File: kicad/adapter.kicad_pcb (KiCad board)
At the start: 16 copper layers, 22 x 31 mm, 14 parts

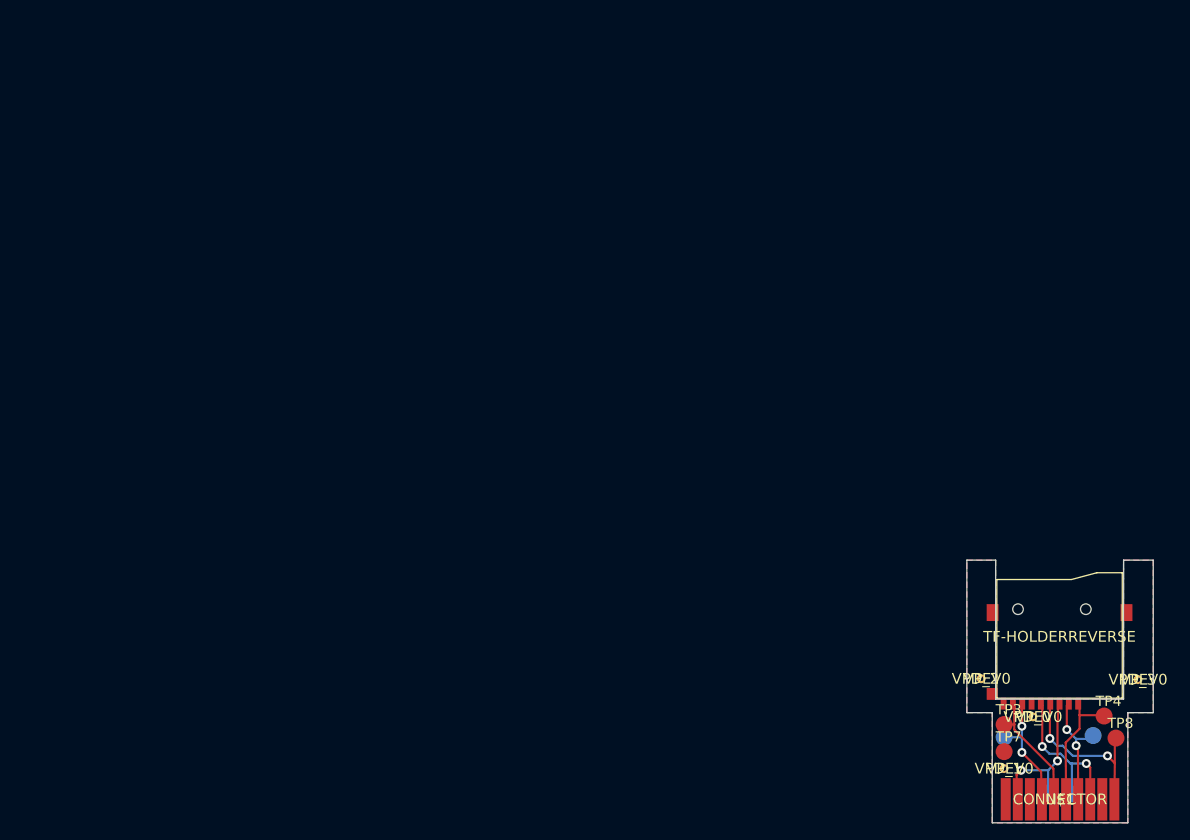
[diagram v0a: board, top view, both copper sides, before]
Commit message: Clean up automatically converted schematic.
Also generate new gerbers.
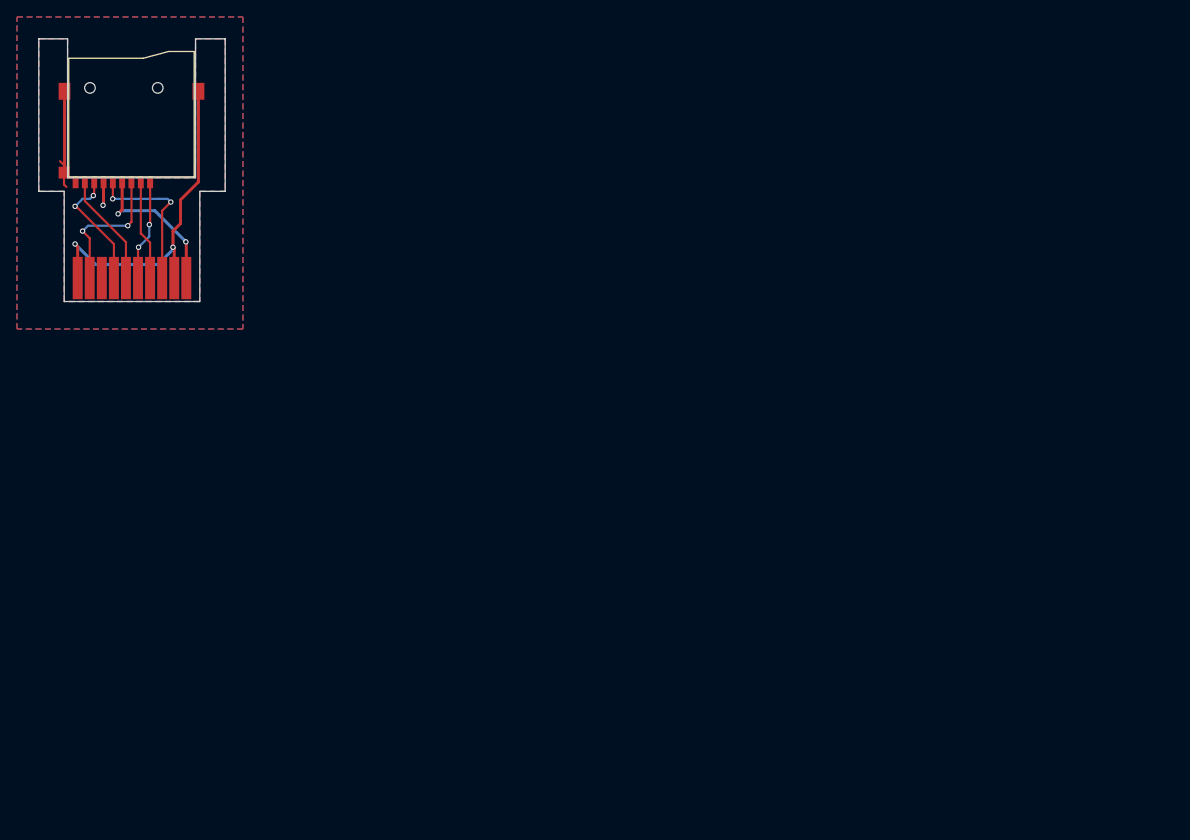
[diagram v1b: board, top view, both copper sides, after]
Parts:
- removed TP1, TP2, TP3, TP4, TP5, TP6, TP7, TP8: TPTP20R, TP20R
- removed VP_0, VP_1, VP_2, VP_3: VPDEV0, VPAC0
- C1: renamed from U$1; footprint CONNECTOR -> adapter:CONNECTOR
- moved C1 125.6 mm to (39.0, 56.2)
- moved SD1 125.6 mm to (38.9, 37.0)
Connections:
- SD1 pad 1: N$7 -> /DAT2
- SD1 pad 2: N$8 -> /DAT3
- SD1 pad 3: N$3 -> /CMD
- SD1 pad 4: N$1 -> /VCC
- SD1 pad 5: N$9 -> /CLK
- SD1 pad 7: N$5 -> /DAT0
- SD1 pad 8: N$6 -> /DAT1
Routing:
- net GND: track 0.00 -> 56.7 mm, vias 0 -> 3
- net N$1: track 20.3 -> 0.00 mm, vias 2 -> 0
- net N$9: track 19.2 -> 0.00 mm, vias 2 -> 0
- net /VCC: track 0.00 -> 18.8 mm, vias 0 -> 2
- net /CLK: track 0.00 -> 18.4 mm, vias 0 -> 2
- net N$3: track 18.0 -> 0.00 mm, vias 2 -> 0
- net /CMD: track 0.00 -> 16.8 mm, vias 0 -> 2
- net N$7: track 15.0 -> 0.00 mm
- net /DAT0: track 0.00 -> 14.7 mm, vias 0 -> 2
- net N$6: track 14.5 -> 0.00 mm
- net N$5: track 14.4 -> 0.00 mm, vias 2 -> 0
- net N$8: track 14.1 -> 0.00 mm, vias 2 -> 0
- net /DAT1: track 0.00 -> 13.3 mm
- net /DAT2: track 0.00 -> 11.9 mm, vias 0 -> 2
- net /DAT3: track 0.00 -> 11.7 mm
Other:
- net class Default: clearance 0.2 -> 0.2032; trace_width 0.25 -> 0.254; via_dia 0.6 -> 0.635; via_drill 0.4 -> 0.381
- net class Power added: clearance 0.2032, trace_width 0.3556, via_dia 0.635, via_drill 0.381
- rule trace_clearance: 0.2 -> 0.2032
- board text removed: "FillOverPAD:GND:10:30"
- board text removed: "FillOverPAD:GND:11:30"
- board text removed: "FillOverPAD:GND:12:30"
- board text removed: "FillOverPAD:GND:19:30"
- board text removed: "FillOverPAD:GND:27:30"
- board text removed: "FillOverPAD:GND:28:30"
- board text removed: "FillOverPAD:GND:29:30"
- board text removed: "FillOverPAD:GND:6:30"
- board text removed: "V:GND:1:4"
- board text removed: "V:GND:2:4"
- board text removed: "V:GND:3:4"
- board text removed: "V:GND:4:4"

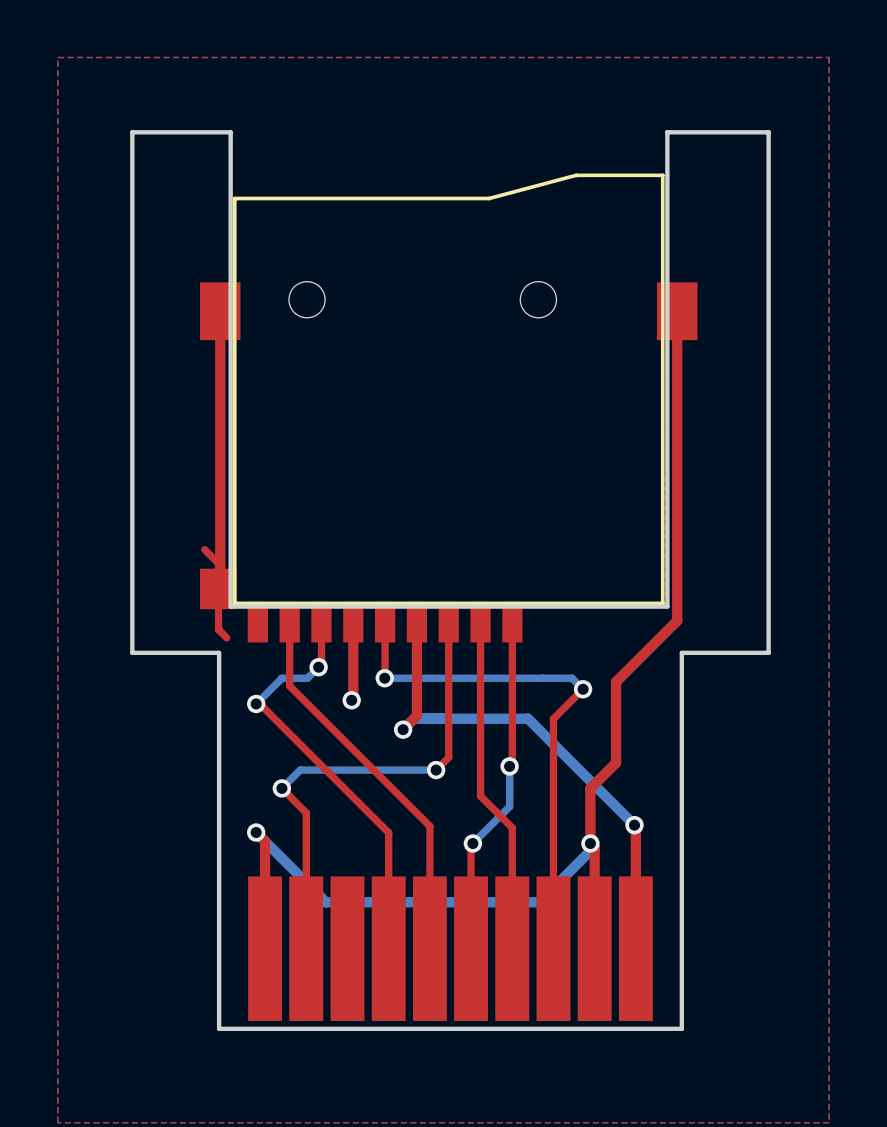
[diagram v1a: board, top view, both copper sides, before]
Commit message: Add fourth mechanical connection for SD slot.
Plus fill keepout around connector pins.
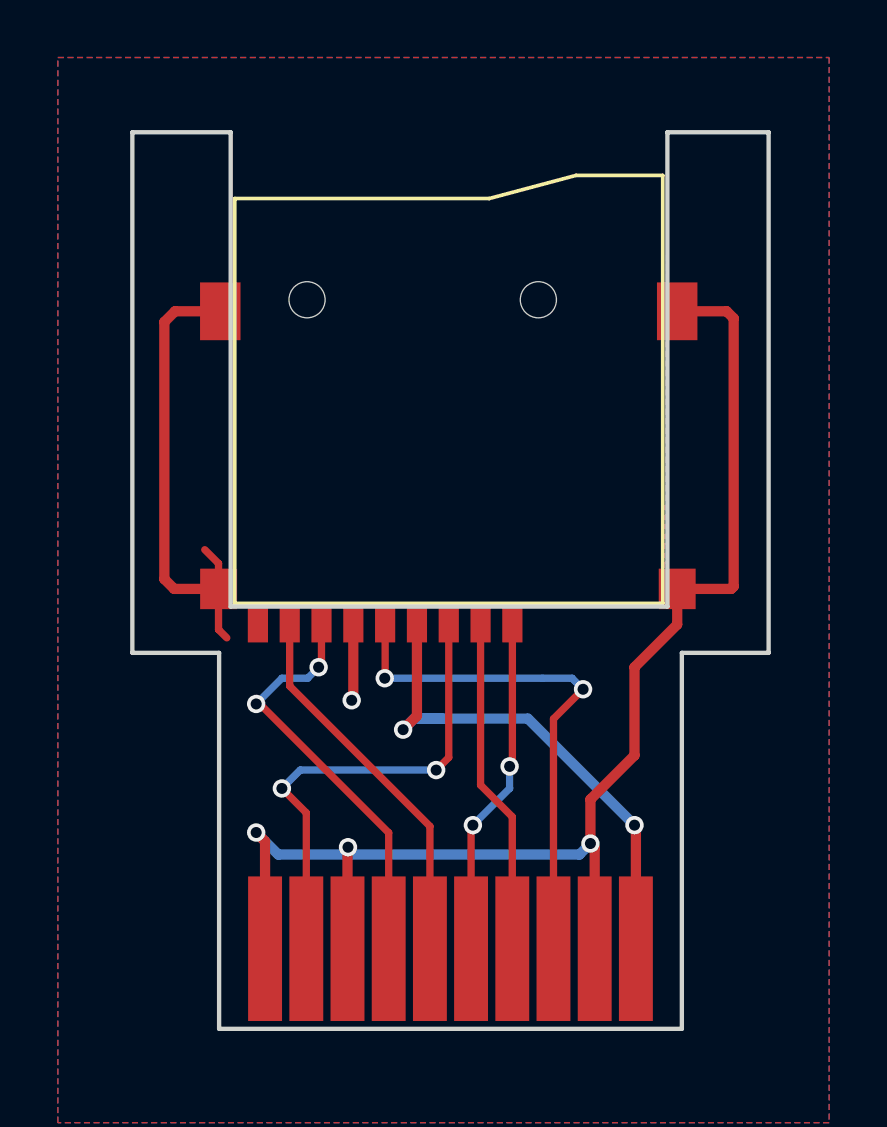
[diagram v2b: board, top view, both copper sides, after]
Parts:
- SD1: footprint TF-PULL-REVERSE -> adapter:TF-PULL-REVERSE
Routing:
- net GND: track 56.7 -> 65.9 mm, vias 3 -> 4

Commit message: refresh gerbers
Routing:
- net /DAT2: track 11.9 -> 12.6 mm
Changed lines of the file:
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@@
     (thickness 1.6)
     (drawings 12)
-    (tracks 89)
+    (tracks 90)
     (zones 0)
     (modules 2)
@@
   (gr_line (start 31.3763 44.3848) (end 46.4763 44.3848) (layer Edge.Cuts) (width 0.15))
   (gr_line (start 46.4763 44.3848) (end 46.4763 27.9848) (layer Edge.Cuts) (width 0.15))
-  (segment (start 35.41522 56.2148) (end 35.41522 52.72278) (width 0.3556) (layer Top) (net 1) (status 400000))
+  (segment (start 35.41522 56.2148) (end 35.41522 52.72278) (width 0.3556) (layer Top) (net 1))
   (via (at 35.433 52.705) (size 0.635) (drill 0.381) (layers Top Bottom) (net 1))
   (segment (start 35.41522 52.72278) (end 35.433 52.705) (width 0.3556) (layer Top) (net 1))
@@
   (segment (start 30.9563 43.7748) (end 30.9563 45.1803) (width 0.254) (layer Top) (net 1) (status 10))
   (segment (start 30.9563 45.1803) (end 31.242 45.466) (width 0.254) (layer Top) (net 1))
-  (segment (start 39.6875 56.2148) (end 39.6875 52.0065) (width 0.254) (layer Top) (net 2))
+  (segment (start 39.6875 56.2148) (end 39.6875 52.2605) (width 0.254) (layer Top) (net 2) (status 400000))
+  (segment (start 41.021 50.927) (end 41.021 49.911) (width 0.254) (layer Bottom) (net 2))
+  (segment (start 39.751 52.197) (end 41.021 50.927) (width 0.254) (layer Bottom) (net 2))
+  (via (at 39.751 52.197) (size 0.635) (drill 0.381) (layers Top Bottom) (net 2))
+  (segment (start 39.6875 52.2605) (end 39.751 52.197) (width 0.254) (layer Top) (net 2))
   (segment (start 41.021 50.673) (end 41.021 49.911) (width 0.254) (layer Bottom) (net 2))
-  (segment (start 39.751 51.943) (end 41.021 50.673) (width 0.254) (layer Bottom) (net 2))
-  (via (at 39.751 51.943) (size 0.635) (drill 0.381) (layers Top Bottom) (net 2))
-  (segment (start 39.6875 52.0065) (end 39.751 51.943) (width 0.254) (layer Top) (net 2))
   (segment (start 41.1163 49.8157) (end 41.1163 44.9248) (width 0.254) (layer Top) (net 2) (status 20))
   (via (at 41.021 49.911) (size 0.635) (drill 0.381) (layers Top Bottom) (net 2))

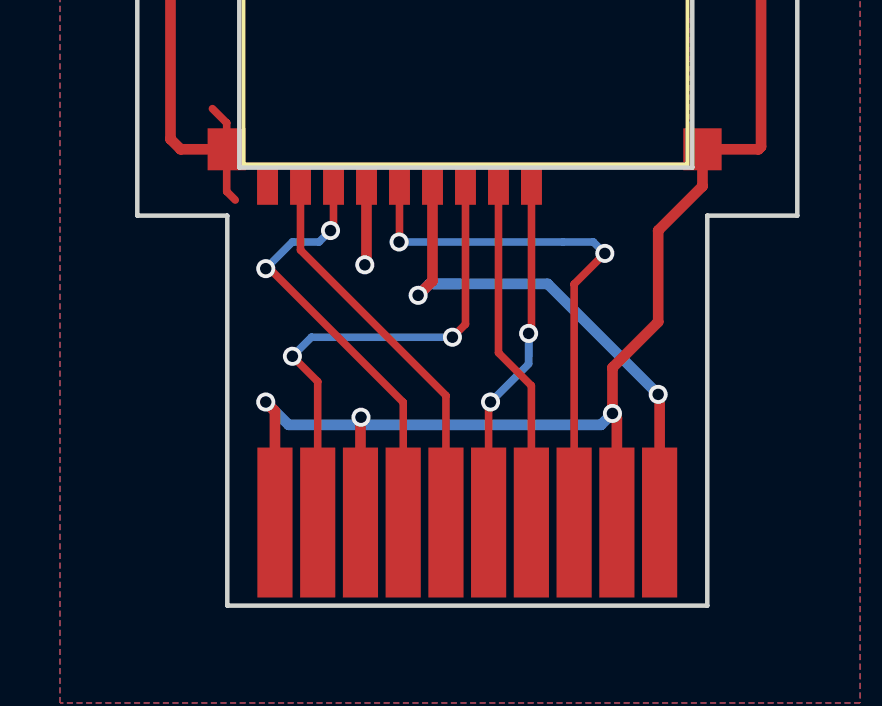
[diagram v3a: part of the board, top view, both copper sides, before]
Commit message: length matching
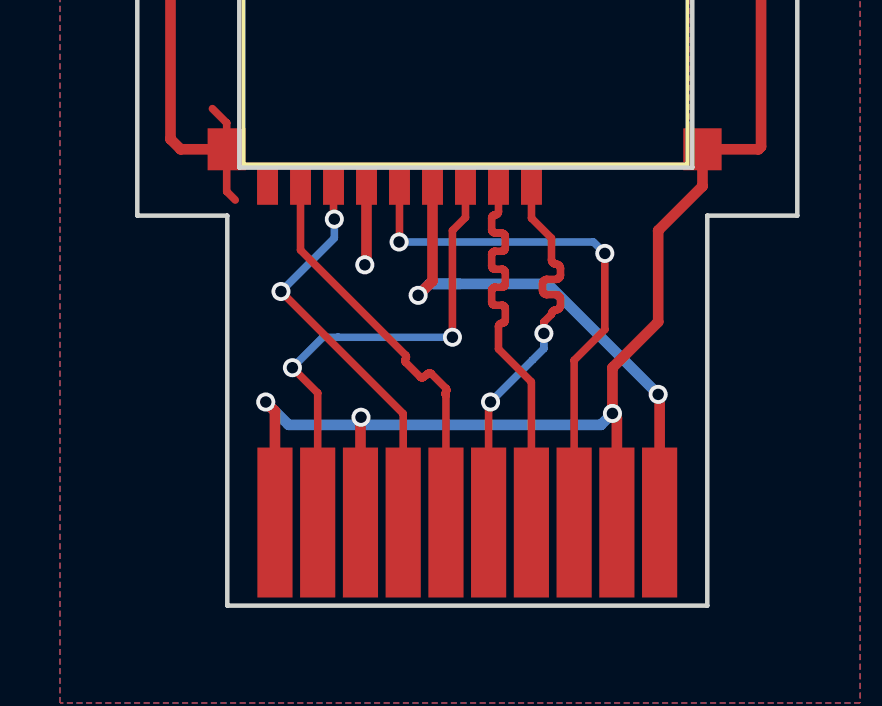
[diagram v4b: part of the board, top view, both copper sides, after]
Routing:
- net /DAT3: track 11.7 -> 13.8 mm
- net /DAT2: track 12.6 -> 13.7 mm
- net /DAT0: track 14.7 -> 13.7 mm
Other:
- copper layers 16 -> 2
